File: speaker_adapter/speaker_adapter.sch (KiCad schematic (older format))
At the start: 4 parts, among them J1 SPK_P, J2 SPK_N, J3 SPK_P, J4 SPK_N

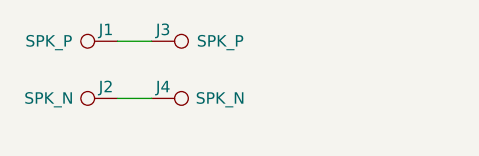
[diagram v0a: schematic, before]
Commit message: Updated speaker adapter to better reflect reality
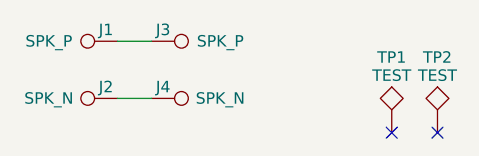
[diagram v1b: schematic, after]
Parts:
- added TP1, TP2: TEST, Measurement_Points:Measurement_Point_Round-TH_Small, symbol TEST
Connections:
- no-connect marks 0 -> 2
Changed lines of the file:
@@
 LIBS:contrib
 LIBS:valves
+LIBS:speaker_adapter-cache
 EELAYER 25 0
 EELAYER END
@@
 Wire Wire Line
 	3550 2900 3700 2900
+$Comp
+L TEST TP1
+U 1 1 5AC14567
+P 4750 3050
+F 0 "TP1" H 4750 3350 50  0000 C BNN
+F 1 "TEST" H 4750 3300 50  0000 C CNN
+F 2 "Measurement_Points:Measurement_Point_Round-TH_Small" H 4750 3050 50  0001 C CNN
+F 3 "" H 4750 3050 50  0001 C CNN
+	1    4750 3050
+	1    0    0    -1
+$EndComp
+$Comp
+L TEST TP2
+U 1 1 5AC145AB
+P 4950 3050
+F 0 "TP2" H 4950 3350 50  0000 C BNN
+F 1 "TEST" H 4950 3300 50  0000 C CNN
+F 2 "Measurement_Points:Measurement_Point_Round-TH_Small" H 4950 3050 50  0001 C CNN
+F 3 "" H 4950 3050 50  0001 C CNN
+	1    4950 3050
+	1    0    0    -1
+$EndComp
+NoConn ~ 4750 3050
+NoConn ~ 4950 3050
 $EndSCHEMATC

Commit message: Started KiCad 5 migration
Opened each schematic, "rescued" symbols, then saved the files. No .kicad_pcb file changes so far.
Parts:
- J1, J2, J3, J4: symbol TEST_1P -> speaker_adapter-rescue:TEST_1P
- TP1, TP2: symbol TEST -> speaker_adapter-rescue:TEST
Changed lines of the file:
@@
-EESchema Schematic File Version 2
-LIBS:power
-LIBS:device
-LIBS:switches
-LIBS:relays
-LIBS:motors
-LIBS:transistors
-LIBS:conn
-LIBS:linear
-LIBS:regul
-LIBS:74xx
-LIBS:cmos4000
-LIBS:adc-dac
-LIBS:memory
-LIBS:xilinx
-LIBS:microcontrollers
-LIBS:dsp
-LIBS:microchip
-LIBS:analog_switches
-LIBS:motorola
-LIBS:texas
-LIBS:intel
-LIBS:audio
-LIBS:interface
-LIBS:digital-audio
-LIBS:philips
-LIBS:display
-LIBS:cypress
-LIBS:siliconi
-LIBS:opto
-LIBS:atmel
-LIBS:contrib
-LIBS:valves
+EESchema Schematic File Version 4
 LIBS:speaker_adapter-cache
-EELAYER 25 0
+EELAYER 26 0
 EELAYER END
 $Descr A4 11693 8268
@@
 $EndDescr
 $Comp
-L TEST_1P J1
+L speaker_adapter-rescue:TEST_1P J1
 U 1 1 5ABE3154
 P 3550 2650
@@
 $EndComp
 $Comp
-L TEST_1P J2
+L speaker_adapter-rescue:TEST_1P J2
 U 1 1 5ABE317F
 P 3550 2900
@@
 $EndComp
 $Comp
-L TEST_1P J3
+L speaker_adapter-rescue:TEST_1P J3
 U 1 1 5ABE319F
 P 3700 2650
@@
 $EndComp
 $Comp
-L TEST_1P J4
+L speaker_adapter-rescue:TEST_1P J4
 U 1 1 5ABE31E0
 P 3700 2900
@@
 	3550 2900 3700 2900
 $Comp
-L TEST TP1
+L speaker_adapter-rescue:TEST TP1
 U 1 1 5AC14567
 P 4750 3050
@@
 $EndComp
 $Comp
-L TEST TP2
+L speaker_adapter-rescue:TEST TP2
 U 1 1 5AC145AB
 P 4950 3050
